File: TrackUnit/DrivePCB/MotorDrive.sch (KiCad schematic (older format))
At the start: 44 parts, among them U1 PIC16(L)F1847-I/P

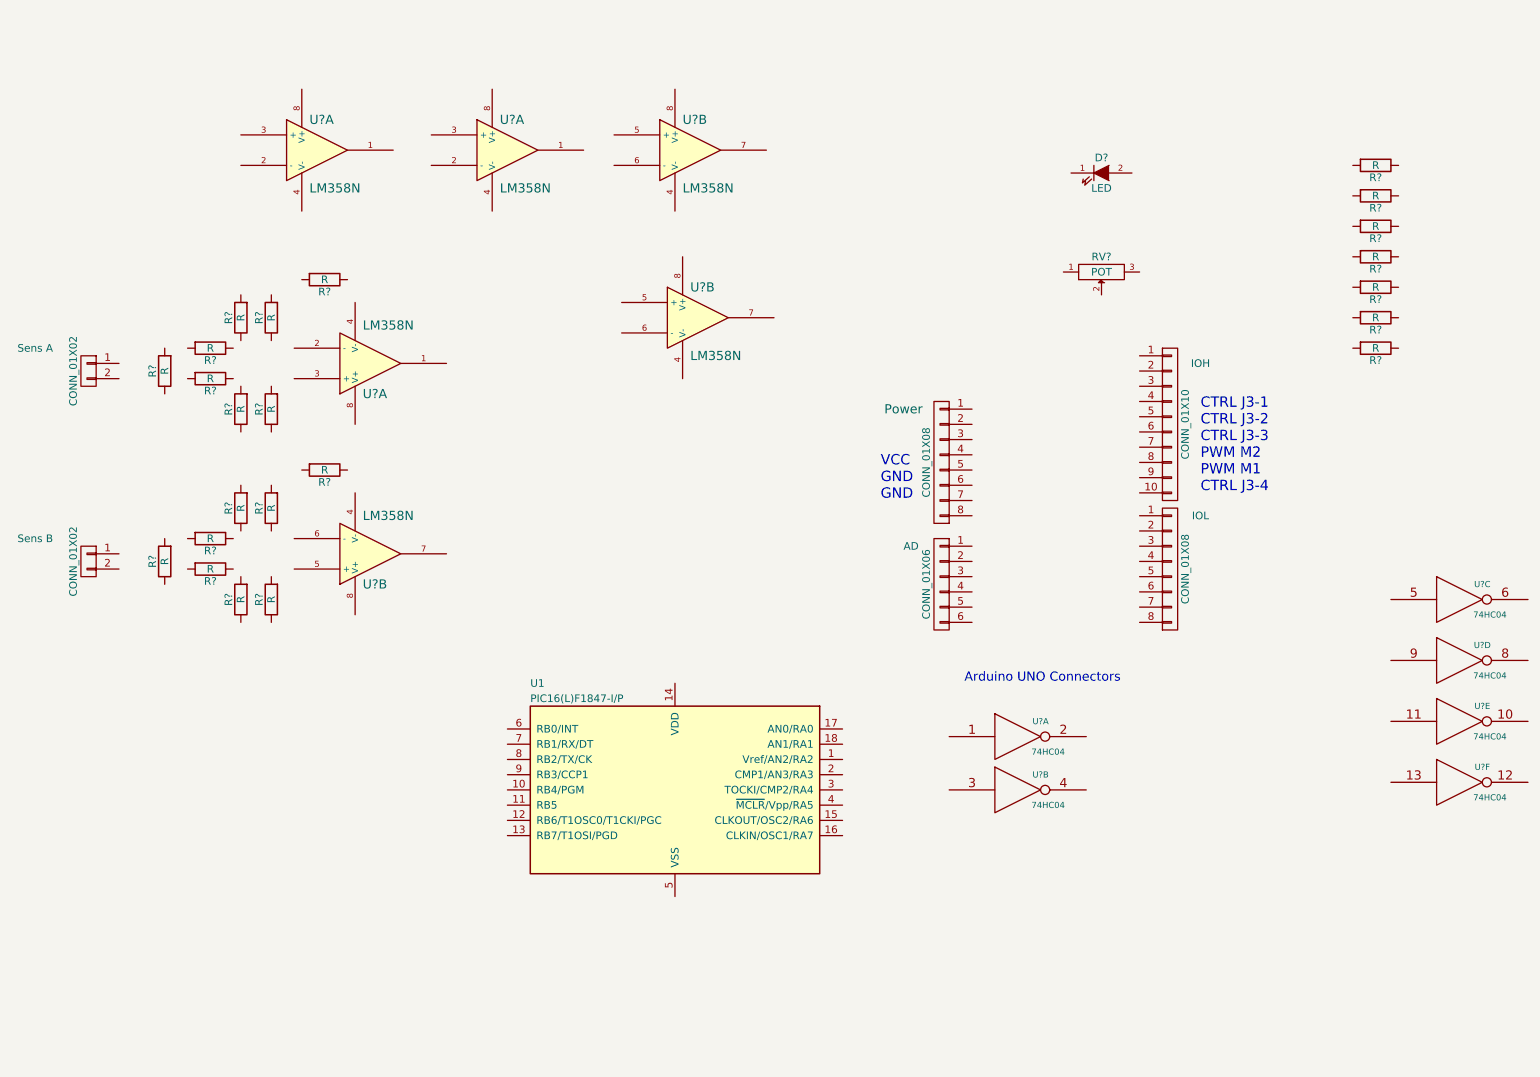
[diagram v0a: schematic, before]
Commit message: PCB Ordered
PCB for drive control is done.
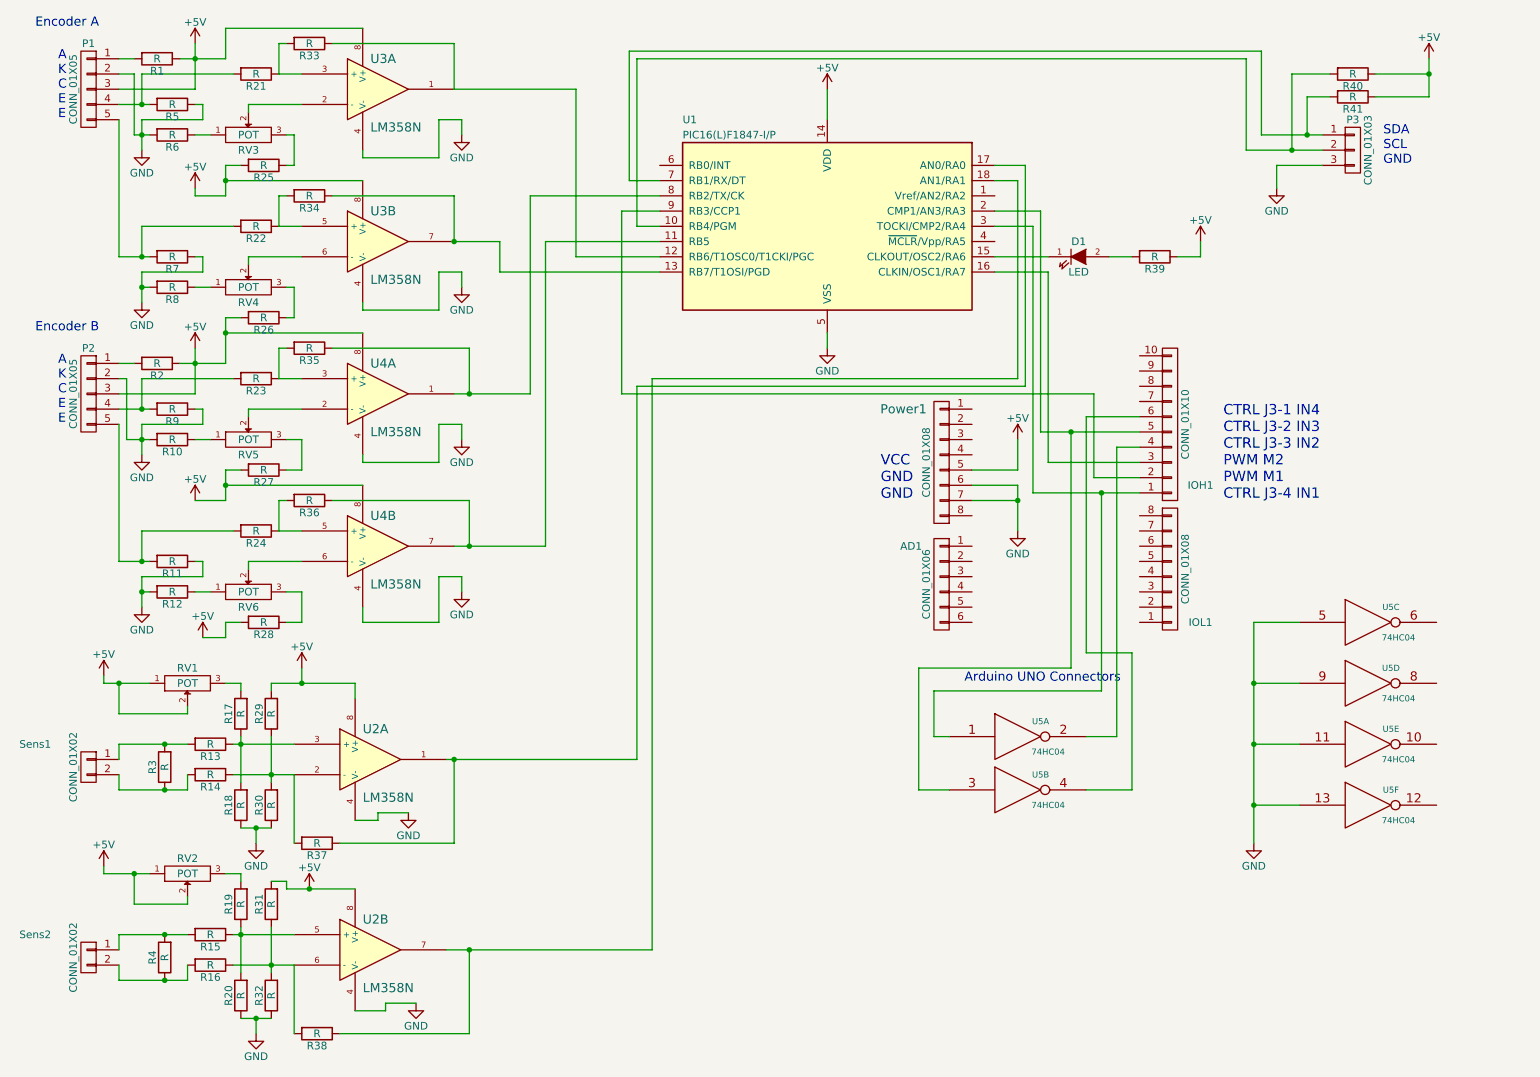
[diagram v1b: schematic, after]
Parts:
- removed R?: R, symbol R
- added P1, P2: CONN_01X05, Pin_Headers:Pin_Header_Straight_1x05, symbol CONN_01X05
- added P3: CONN_01X03, Pin_Headers:Pin_Header_Straight_1x03, symbol CONN_01X03
- added R10, R11, R12, R21, R22, R23, R24, R25, R26, R27, R28, R33, R34, R35, R36, R5, R6, R7, R9: R, Resistors_SMD:R_0805_HandSoldering, symbol R
- added RV2, RV3, RV4, RV5, RV6: POT, Potentiometers:Potentiometer_Bourns_3296W_3-8Zoll_Inline_ScrewUp, symbol POT
- AD1: renamed from AD; footprint (none) -> Pin_Headers:Pin_Header_Straight_1x06
- D1: renamed from D?; footprint (none) -> LEDs:LED-1206
- IOH1: renamed from IOH; footprint (none) -> Pin_Headers:Pin_Header_Straight_1x10
- IOL1: renamed from IOL; footprint (none) -> Pin_Headers:Pin_Header_Straight_1x08
- Power1: renamed from Power; footprint (none) -> Pin_Headers:Pin_Header_Straight_1x08
- R1, R13, R14, R15, R16, R17, R18, R19, R2, R20, R29, R3, R30, R31, R32, R37, R38, R39, R4, R40, R41, R8: renamed from R?; footprint (none) -> Resistors_SMD:R_0805_HandSoldering
- RV1: renamed from RV?; footprint (none) -> Potentiometers:Potentiometer_Bourns_3296W_3-8Zoll_Inline_ScrewUp
- Sens1, Sens2: renamed from Sens; footprint (none) -> Pin_Headers:Pin_Header_Straight_1x02
- U1: footprint (none) -> Housings_DIP:DIP-18_W7.62mm_LongPads
- U2, U3, U4: renamed from U?; footprint (none) -> Housings_SOIC:SOIC-8_3.9x4.9mm_Pitch1.27mm
- U5: renamed from U?; footprint (none) -> SMD_Packages:SOIC-14_N
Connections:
- net GND: now also Power1.6 (P6), Power1.7 (P7), R18.1, R20.1, R30.1, R32.1, R8.2, U1.5 (VSS), U2.4 (V-), U2.4 (V-), U3.4 (V-), U3.4 (V-), U4.4 (V-), U4.4 (V-), U5.11, U5.13, U5.5, U5.9, P1.2 (P2), P2.2 (P2), P3.3 (P3), R10.2, R11.1, R12.2, R5.1, R6.2, R7.1, R9.1
- net at D1.1 (K): now also U1.15 (CLKOUT/OSC2/RA6)
- net at D1.2 (A): now also R39.2
- net at R3.1: now also R14.2, Sens1.2 (P2)
- net at R3.2: now also R13.2, Sens1.1 (P1)
- net +5V: now reaches RV1.1
- net +5V: now also Power1.5 (P5), R1.1, R2.1, R29.2, R31.2, R39.1, R40.1, R41.1, RV1.2, U1.14 (VDD), U2.8 (V+), U2.8 (V+), U3.8 (V+), U3.8 (V+), U4.8 (V+), U4.8 (V+), P1.3 (P3), P2.3 (P3), R25.2, R26.2, R27.2, R28.2, RV2.1, RV2.2
- net at RV1.3: now also R17.2
- net at U2.5 (+): now also R15.1, R19.1, R20.2
- net at U2.6 (-): now also R16.1, R31.1, R32.2, R38.2
- net at U2.7: now also R38.1, U1.18 (AN1/RA1)
- net at U1.10 (RB4/PGM): now also R40.2, P3.2 (P2)
- net at U1.11 (RB5): now also U4.7, R36.1
- net at U1.12 (RB6/T1OSC0/T1CKI/PGC): now also U3.1, R33.1
- net at U1.13 (RB7/T1OSI/PGD): now also U3.7, R34.1
- net at U1.16 (CLKIN/OSC1/RA7): now also IOH1.3 (P3)
- net at U1.17 (AN0/RA0): now also R37.1, U2.1
- net at U1.2 (CMP1/AN3/RA3): now also IOH1.5 (P5), U5.3
- net at U1.3 (TOCKI/CMP2/RA4): now also IOH1.1 (P1), U5.1
- net at U1.7 (RB1/RX/DT): now also R41.2, P3.1 (P1)
- net at U1.8 (RB2/TX/CK): now also U4.1, R35.1
- net at U1.9 (RB3/CCP1): now also IOH1.2 (P2)
- net at IOH1.4 (P4): now also U5.2
- net at IOH1.6 (P6): now also U5.4
- net at U3.2 (-): now also RV3.2
- net at U3.3 (+): now also R21.1, R33.2
- net at U2.2 (-): now also R14.1, R29.1, R30.2, R37.2
- net at U2.3 (+): now also R13.1, R17.1, R18.2
- net at R4.1: now also R16.2, Sens2.2 (P2)
- net at R4.2: now also R15.2, Sens2.1 (P1)
- net at R1.2: now also P1.1 (P1)
- net at R2.2: now also P2.1 (P1)
- net at R8.1: now also RV4.1
- net at U4.5 (+): now also R24.1, R36.2
- net at U4.6 (-): now also RV6.2
- net at R19.2: now also RV2.3
- new net: R22.1, R34.2, U3.5 (+)
- new net: RV4.2, U3.6 (-)
- new net: RV5.2, U4.2 (-)
- new net: R23.1, R35.2, U4.3 (+)
- new net: R6.1, RV3.1
- new net: R25.1, RV3.3
- new net: R26.1, RV4.3
- new net: R10.1, RV5.1
- new net: R27.1, RV5.3
- new net: R12.1, RV6.1
- new net: R28.1, RV6.3
- new net: P1.4 (P4), R21.2, R5.2
- new net: P1.5 (P5), R22.2, R7.2
- new net: P2.4 (P4), R23.2, R9.2
- new net: P2.5 (P5), R11.2, R24.2
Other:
- note added: "A\nK\nC\nE\nE"
- note added: "CTRL J3-1 IN4\nCTRL J3-2 IN3\nCTRL J3-3 IN2\nPWM M2\nPWM M1\nCTRL J3-4 IN1"
- note added: "Encoder A"
- note added: "Encoder B"
- note added: "SDA\nSCL\nGND\n"
- note removed: "CTRL J3-1\nCTRL J3-2\nCTRL J3-3\nPWM M2\nPWM M1\nCTRL J3-4"
- moved on the sheet: D1, R1, R13, R14, R15, R16, R17, R18, R19, R2, R20, R29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
